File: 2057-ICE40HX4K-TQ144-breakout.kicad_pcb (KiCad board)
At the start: 2 copper layers, 99.1 x 66 mm, 41 parts, among them J1 Conn_02x30_Odd_Even, J2 Conn_02x30_Odd_Even, J3 RaspberryPI-B+header, J4 0548190519, J5 RaspberryPI-B+header, J6 Conn_02x06_Odd_Even, J7 Conn_02x01, U1 ICE40HX4K-TQ144, U2 AZ1117CH-3.3TRG1, U3 AZ1117CH-1.2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

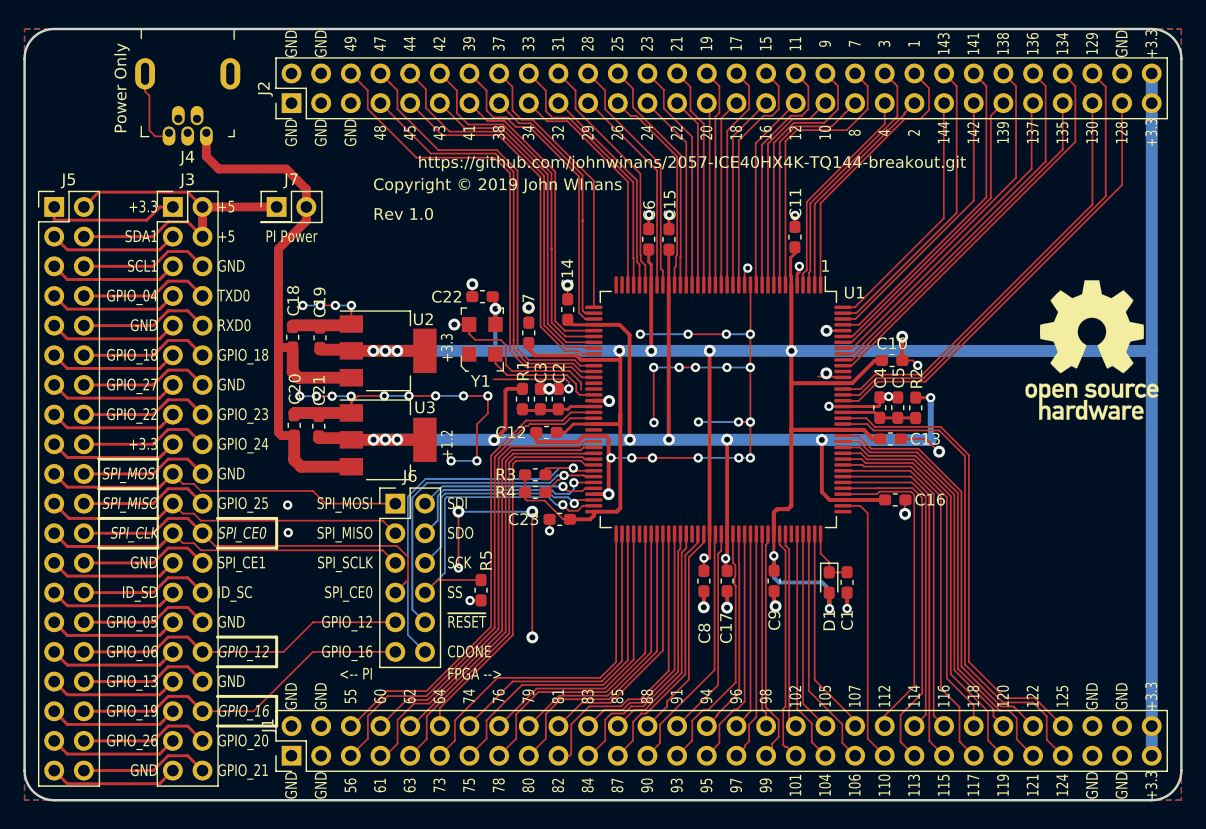
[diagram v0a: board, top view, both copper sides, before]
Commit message: Added some ground vias, schematic PDF & some digikey nos.
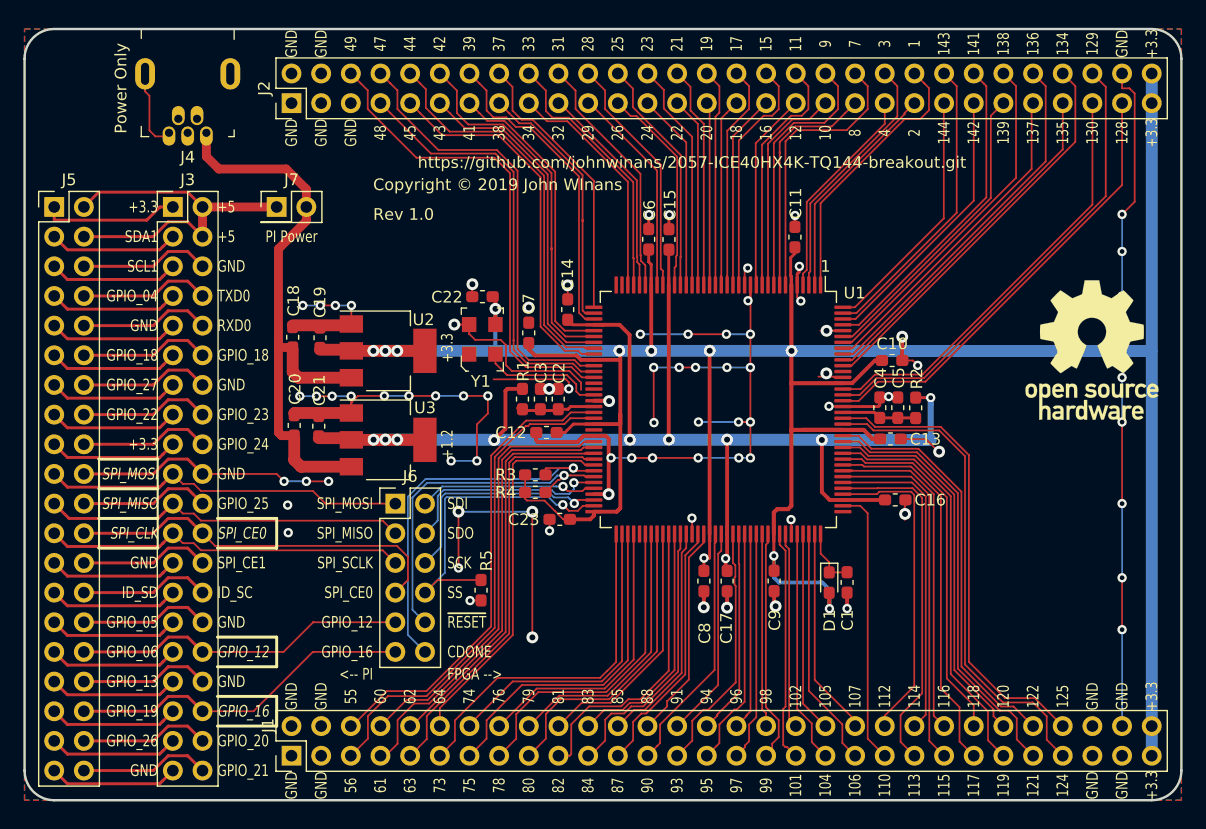
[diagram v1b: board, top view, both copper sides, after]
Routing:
- net GND: track 293.3 -> 363.2 mm, vias 67 -> 83
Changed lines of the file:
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@@
     (thickness 1.6)
     (drawings 208)
-    (tracks 1337)
+    (tracks 1378)
     (zones 0)
     (modules 41)
@@
   (segment (start 72.6948 69.5198) (end 72.6948 71.0184) (width 0.1524) (layer F.Cu) (net 1))
   (segment (start 72.6948 71.0184) (end 71.755 71.9582) (width 0.1524) (layer F.Cu) (net 1))
+  (segment (start 90.1806 81.34308) (end 90.1806 79.9952) (width 0.1524) (layer F.Cu) (net 1))
+  (via (at 90.17 79.9846) (size 0.8) (drill 0.4) (layers F.Cu B.Cu) (net 1))
+  (segment (start 90.1806 79.9952) (end 90.17 79.9846) (width 0.1524) (layer F.Cu) (net 1))
+  (via (at 98.6536 80.1116) (size 0.8) (drill 0.4) (layers F.Cu B.Cu) (net 1))
+  (segment (start 98.6806 81.34308) (end 98.6806 80.1386) (width 0.1524) (layer F.Cu) (net 1))
+  (segment (start 98.6806 80.1386) (end 98.6536 80.1116) (width 0.1524) (layer F.Cu) (net 1))
+  (via (at 99.4918 61.3918) (size 0.8) (drill 0.4) (layers F.Cu B.Cu) (net 1))
+  (segment (start 99.1806 60.01808) (end 99.1806 61.0806) (width 0.1524) (layer F.Cu) (net 1))
+  (segment (start 99.1806 61.0806) (end 99.4918 61.3918) (width 0.1524) (layer F.Cu) (net 1))
+  (via (at 94.9706 61.3664) (size 0.8) (drill 0.4) (layers F.Cu B.Cu) (net 1))
+  (segment (start 95.1806 60.01808) (end 95.1806 61.1564) (width 0.1524) (layer F.Cu) (net 1))
+  (segment (start 95.1806 61.1564) (end 94.9706 61.3664) (width 0.1524) (layer F.Cu) (net 1))
+  (via (at 127 89.535) (size 0.8) (drill 0.4) (layers F.Cu B.Cu) (net 1))
+  (segment (start 127 97.79) (end 127 89.535) (width 0.1524) (layer B.Cu) (net 1))
+  (via (at 127 85.09) (size 0.8) (drill 0.4) (layers F.Cu B.Cu) (net 1))
+  (segment (start 127 89.535) (end 127 85.09) (width 0.1524) (layer F.Cu) (net 1))
+  (via (at 127 78.74) (size 0.8) (drill 0.4) (layers F.Cu B.Cu) (net 1))
+  (segment (start 127 85.09) (end 127 78.74) (width 0.1524) (layer B.Cu) (net 1))
+  (via (at 127 71.755) (size 0.8) (drill 0.4) (layers F.Cu B.Cu) (net 1))
+  (segment (start 127 78.74) (end 127 71.755) (width 0.1524) (layer F.Cu) (net 1))
+  (via (at 127 67.945) (size 0.8) (drill 0.4) (layers F.Cu B.Cu) (net 1))
+  (segment (start 127 71.755) (end 127 67.945) (width 0.1524) (layer B.Cu) (net 1))
+  (segment (start 127 41.91) (end 127 43.18) (width 0.1524) (layer F.Cu) (net 1))
+  (segment (start 127 43.18) (end 127.635 43.18) (width 0.1524) (layer F.Cu) (net 1))
+  (via (at 127 53.975) (size 0.8) (drill 0.4) (layers F.Cu B.Cu) (net 1))
+  (segment (start 128.078601 52.896399) (end 127 53.975) (width 0.1524) (layer F.Cu) (net 1))
+  (segment (start 127.635 43.18) (end 128.078601 43.623601) (width 0.1524) (layer F.Cu) (net 1))
+  (segment (start 128.078601 43.623601) (end 128.078601 52.896399) (width 0.1524) (layer F.Cu) (net 1))
+  (segment (start 127 53.975) (end 127 57.15) (width 0.1524) (layer B.Cu) (net 1))
+  (via (at 127 57.15) (size 0.8) (drill 0.4) (layers F.Cu B.Cu) (net 1))
+  (via (at 127 60.96) (size 0.8) (drill 0.4) (layers F.Cu B.Cu) (net 1))
+  (segment (start 127 57.15) (end 127 60.96) (width 0.1524) (layer B.Cu) (net 1))
+  (via (at 127 64.135) (size 0.8) (drill 0.4) (layers F.Cu B.Cu) (net 1))
+  (segment (start 127 60.96) (end 127 64.135) (width 0.1524) (layer F.Cu) (net 1))
+  (segment (start 48.26 76.2) (end 54.61 76.2) (width 0.1524) (layer F.Cu) (net 1))
+  (via (at 55.245 76.835) (size 0.8) (drill 0.4) (layers F.Cu B.Cu) (net 1))
+  (segment (start 54.61 76.2) (end 55.245 76.835) (width 0.1524) (layer F.Cu) (net 1))
+  (segment (start 55.245 76.835) (end 57.15 76.835) (width 0.1524) (layer B.Cu) (net 1))
+  (via (at 57.15 76.835) (size 0.8) (drill 0.4) (layers F.Cu B.Cu) (net 1))
+  (via (at 59.055 76.835) (size 0.8) (drill 0.4) (layers F.Cu B.Cu) (net 1))
+  (segment (start 57.15 76.835) (end 59.055 76.835) (width 0.1524) (layer F.Cu) (net 1))
   (via (at 73.33996 62.06236) (size 1.016) (drill 0.508) (layers F.Cu B.Cu) (net 10))
   (via (at 91.68384 65.65138) (size 1.016) (drill 0.508) (layers F.Cu B.Cu) (net 10))

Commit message: Fix programming headers, add LEDs, cosmetic fixes.
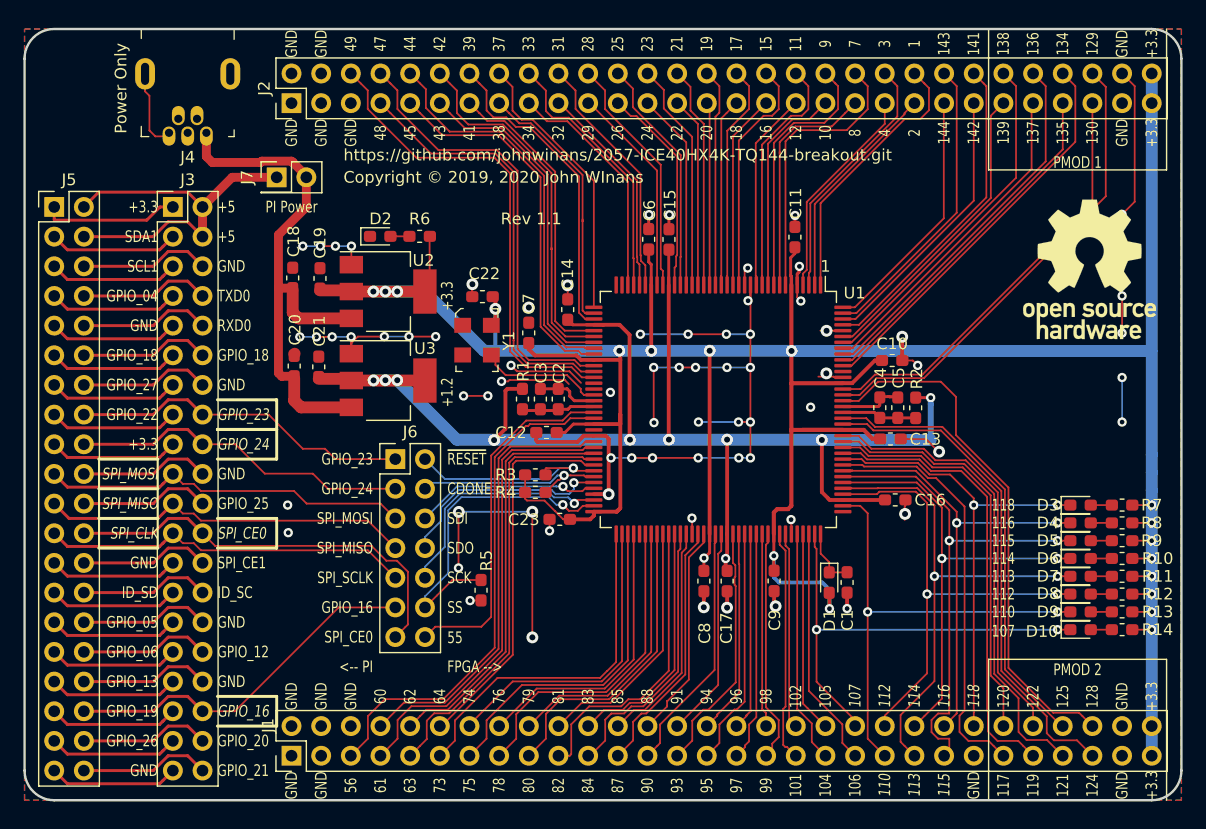
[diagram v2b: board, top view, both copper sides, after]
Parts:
- added D10: LED_ALT, LED_SMD:LED_0603_1608Metric_Pad1.05x0.95mm_HandSolder, F.Cu at (123.4, 89.5)
- added D2: LED_ALT, LED_SMD:LED_0603_1608Metric_Pad1.05x0.95mm_HandSolder, F.Cu at (63.5, 55.9)
- added D3: LED_ALT, LED_SMD:LED_0603_1608Metric_Pad1.05x0.95mm_HandSolder, F.Cu at (123.4, 78.9)
- added D4: LED_ALT, LED_SMD:LED_0603_1608Metric_Pad1.05x0.95mm_HandSolder, F.Cu at (123.4, 80.4)
- added D5: LED_ALT, LED_SMD:LED_0603_1608Metric_Pad1.05x0.95mm_HandSolder, F.Cu at (123.4, 81.9)
- added D6: LED_ALT, LED_SMD:LED_0603_1608Metric_Pad1.05x0.95mm_HandSolder, F.Cu at (123.4, 83.4)
- added D7: LED_ALT, LED_SMD:LED_0603_1608Metric_Pad1.05x0.95mm_HandSolder, F.Cu at (123.4, 85.0)
- added D8: LED_ALT, LED_SMD:LED_0603_1608Metric_Pad1.05x0.95mm_HandSolder, F.Cu at (123.4, 86.5)
- added D9: LED_ALT, LED_SMD:LED_0603_1608Metric_Pad1.05x0.95mm_HandSolder, F.Cu at (123.4, 88.0)
- added R10: 330, Resistor_SMD:R_0603_1608Metric_Pad1.05x0.95mm_HandSolder, F.Cu at (127.0, 83.4)
- added R11: 330, Resistor_SMD:R_0603_1608Metric_Pad1.05x0.95mm_HandSolder, F.Cu at (127.0, 85.0)
- added R12: 330, Resistor_SMD:R_0603_1608Metric_Pad1.05x0.95mm_HandSolder, F.Cu at (127.0, 86.5)
- added R13: 330, Resistor_SMD:R_0603_1608Metric_Pad1.05x0.95mm_HandSolder, F.Cu at (127.0, 88.0)
- added R14: 330, Resistor_SMD:R_0603_1608Metric_Pad1.05x0.95mm_HandSolder, F.Cu at (127.0, 89.5)
- added R6: 330, Resistor_SMD:R_0603_1608Metric_Pad1.05x0.95mm_HandSolder, F.Cu at (66.9, 55.9)
- added R7: 330, Resistor_SMD:R_0603_1608Metric_Pad1.05x0.95mm_HandSolder, F.Cu at (127.0, 78.9)
- added R8: 330, Resistor_SMD:R_0603_1608Metric_Pad1.05x0.95mm_HandSolder, F.Cu at (127.0, 80.4)
- added R9: 330, Resistor_SMD:R_0603_1608Metric_Pad1.05x0.95mm_HandSolder, F.Cu at (127.0, 81.9)
- J6: value Conn_02x06_Odd_Even -> Conn_02x07_Odd_Even; footprint Connector_PinHeader_2.54mm:PinHeader_2x06_P2.54mm_Vertical -> Connector_PinHeader_2.54mm:PinHeader_2x07_P2.54mm_Vertical
- Y1: footprint digikey-footprints:Oscillator_XLH536025.000000I -> jb-footprint:Oscillator_XLH536025.000000I
- moved LOGO1 6.91 mm to (124.2, 58.7)
- moved C20 5.08 mm to (56.1, 67.0)
- moved U3 5.08 mm to (64.2, 68.2)
- moved C18 5.08 mm to (56.0, 59.4)
- moved U2 5.08 mm to (64.2, 60.6)
- moved C19 5.08 mm to (58.3, 59.5)
- moved C21 5.08 mm to (58.2, 67.0)
- moved J6 3.81 mm to (64.8, 74.9)
- moved Y1 3.66 mm to (70.6, 63.5), turned to 270 degrees
- moved J7 2.54 mm to (54.6, 50.8)
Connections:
- C2 pad 2: GND -> Net-(C2-Pad2)
- C3 pad 2: GND -> Net-(C2-Pad2)
- C4 pad 2: GND -> Net-(C4-Pad2)
- C5 pad 2: GND -> Net-(C4-Pad2)
- J1 pad 47: /IOT_174 -> GND
- J1 pad 49: /IOT_178 -> /IOT_174
- J1 pad 51: /IOT_181 -> /IOT_178
- J1 pad 53: /IOT_191 -> /IOT_181
- J1 pad 55: GND -> /IOT_191
- J1 pad 56: GND -> /IOT_197
- J1 pad 6: /IOB_91 -> GND
- J2 pad 57: /IOT_197 -> GND
- J6 pad 1: /SPI_MOSI -> /GPIO23
- J6 pad 10: /~CRESET~ -> /IOB_107_SCK
- J6 pad 12: /CDONE -> /IOB_108_SS
- J6 pad 2: /IOB_106_SDI -> /CDONE
- J6 pad 3: /SPI_MISO -> /GPIO24
- J6 pad 4: /IOB_105_SDO -> /~CRESET~
- J6 pad 5: /SPI_SCLK -> /SPI_MOSI
- J6 pad 6: /IOB_107_SCK -> /IOB_106_SDI
- J6 pad 7: /SPI_CE0 -> /SPI_MISO
- J6 pad 8: /IOB_108_SS -> /IOB_105_SDO
- J6 pad 9: /GPIO12 -> /SPI_SCLK
- U1 pad 127: GND -> Net-(C4-Pad2)
- U1 pad 53: GND -> Net-(C2-Pad2)
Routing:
- net GND: track 363.2 -> 283.9 mm, vias 83 -> 73
- net /IOR_167: track 17.9 -> 39.6 mm, vias 0 -> 2
- net +3V3: track 268.1 -> 288.1 mm, vias 11 -> 19
- net /GPIO24: track 11.2 -> 29.3 mm
- net /GPIO23: track 11.2 -> 29.3 mm
- net /GPIO12: track 28.8 -> 11.2 mm
- net /IOT_168: track 23.8 -> 41.1 mm, vias 0 -> 2
- net /CDONE: track 33.9 -> 18.6 mm
- net /IOT_169: track 27.2 -> 40.6 mm, vias 0 -> 2
- net /IOT_172: track 30.9 -> 44.3 mm, vias 0 -> 2
- net /IOT_170: track 31.2 -> 44.0 mm, vias 0 -> 2
- net /~CRESET~: track 29.7 -> 17.2 mm
- net /IOT_171: track 27.7 -> 40.0 mm, vias 0 -> 2
- net /IOT_173: track 29.7 -> 40.5 mm, vias 0 -> 2
- net /IOB_91: track 40.5 -> 30.5 mm
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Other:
- board text added: "Copyright © 2019, 2020 John WInans"
- board text added: "PMOD 1"
- board text added: "PMOD 2"
- board text added: "Rev 1.1"
- board text removed: "Copyright © 2019 John WInans"
- board text removed: "Rev 1.0"

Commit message: Added two pushbuttons.
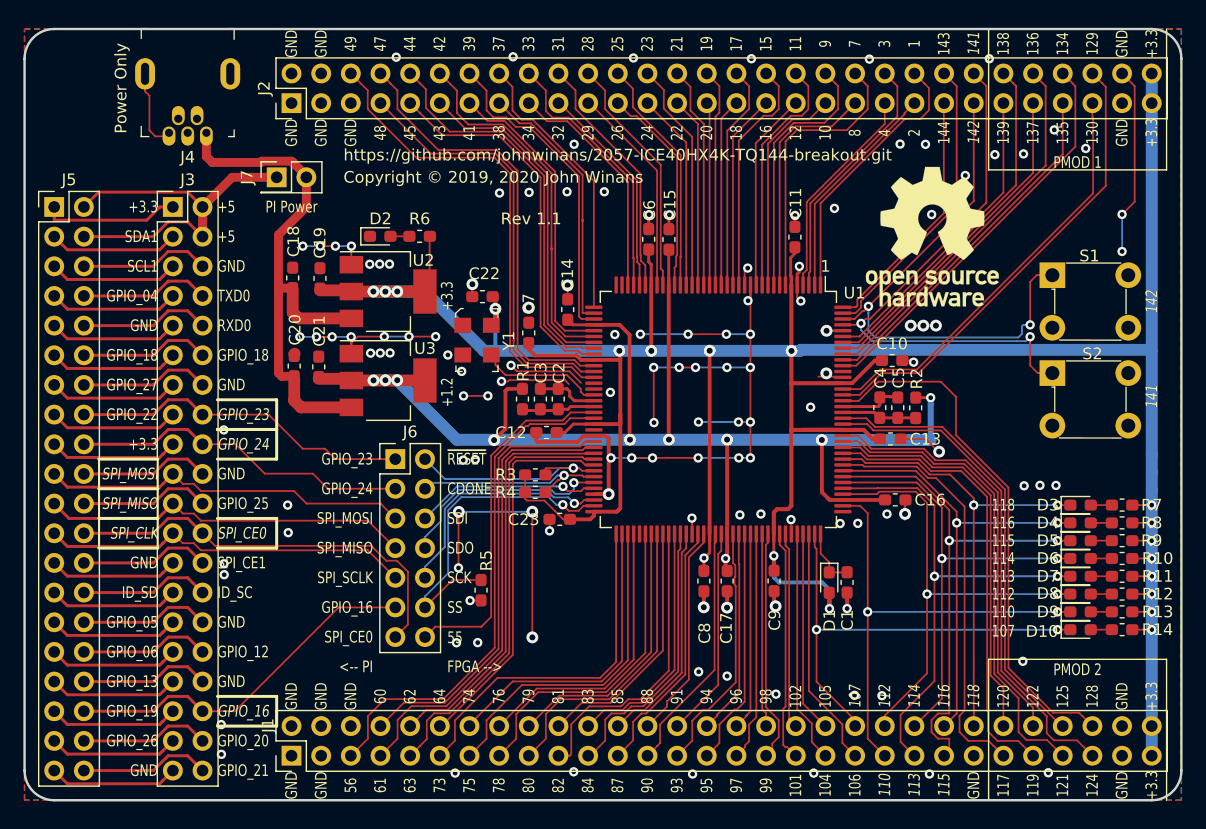
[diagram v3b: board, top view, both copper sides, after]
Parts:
- added S1: 1825910-6, digikey-footprints:Switch_Tactile_THT_6x6mm, F.Cu at (121.0, 59.2)
- added S2: 1825910-6, digikey-footprints:Switch_Tactile_THT_6x6mm, F.Cu at (121.0, 67.6)
- moved LOGO1 13.7 mm to (110.7, 55.9)
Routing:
- net /IOT_220: track 23.8 -> 46.6 mm, vias 0 -> 2
- net /IOT_219: track 27.9 -> 48.4 mm, vias 0 -> 2
- net GND: track 283.9 -> 272.8 mm, vias 73 -> 129
- net /IOT_198: track 40.6 -> 40.0 mm
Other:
- board text added: "Copyright © 2019, 2020 John Winans"
- board text removed: "Copyright © 2019, 2020 John WInans"

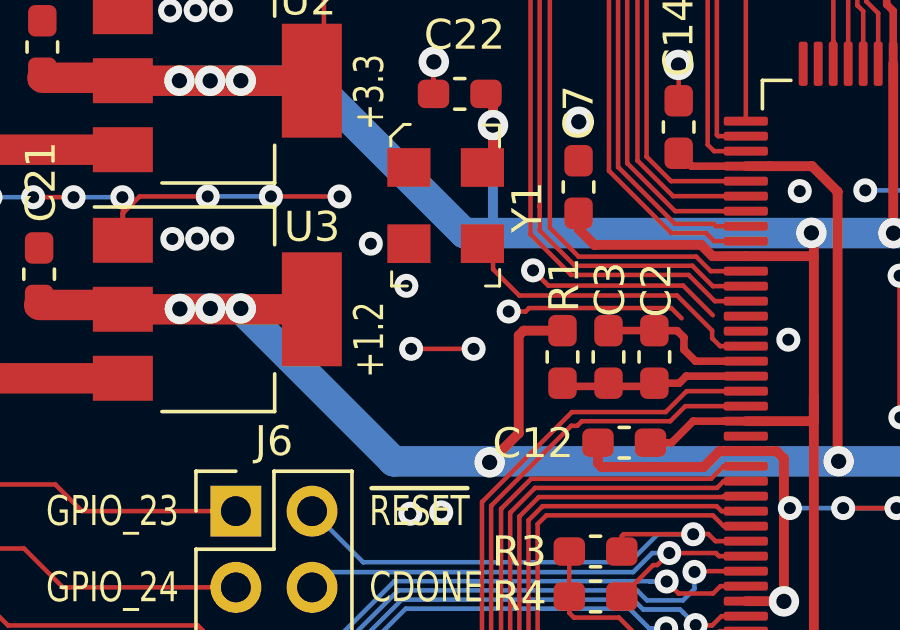
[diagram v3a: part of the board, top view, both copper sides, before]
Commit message: Spec D1 as: 1N4448WSF-7 & label clock on pin 55
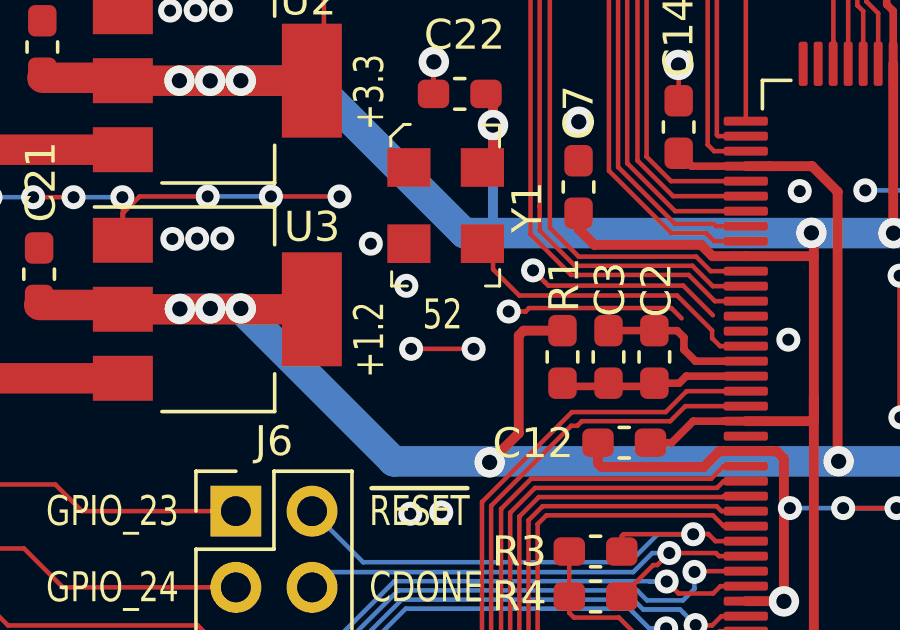
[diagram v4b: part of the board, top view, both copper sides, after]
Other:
- board text added: "52"
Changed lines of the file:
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@@
   (general
     (thickness 1.6)
-    (drawings 234)
+    (drawings 235)
     (tracks 1562)
     (zones 0)
@@
     )
   )
+  (gr_text 52 (at 70.993 68.3768) (layer F.SilkS)
+    (effects (font (size 1 0.762) (thickness 0.15)) (justify left))
+  )
   (gr_text 142 (at 129.54 61.468 90) (layer F.SilkS)
